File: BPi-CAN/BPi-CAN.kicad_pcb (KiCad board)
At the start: 2 copper layers, 100 x 100 mm, 123 parts, among them J1 RJ45, J2 RJ45, J3 RJ45, J4 RJ45, P1 BPi, P10 SPI, P11 SNIFFER, P12 CAN-Bus, P13 USB, P14 CAN-Bus, P15 POWER, P16 CAN, P17 CAN, P18 CAN, P19 TERM, P2 S88, P20 S88 CONN, P21 RS232 Con, P22 S88, P23 CONN_01X08, P24 CONN_01X03, P25 I2C-Bus, P3 CONN_02X04, P4 BPi Con, P5 TERM, P6 S88, P7 I2C-Bus, P8 RS485, P9 RS232, U1 MCP2562, U10 MCP2562, U11 6N137, U12 ISO1050, U13 FT230XS, U2 LM7805, U3 6N137, U4 6N137, U5 6N137, U6 6N137, U7 ADuM1251BR, U8 MAX3072E, U9 MAX3232

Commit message: small changes : mainly text
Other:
- board text added: "G"
- board text added: "V"
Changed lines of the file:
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@@
   (general
     (links 282)
-    (no_connects 0)
-    (area 86.872087 28.15 207.5 148.200001)
+    (no_connects 26)
+    (area 99.924999 39.924999 200.075001 140.075001)
     (thickness 1.6)
-    (drawings 101)
+    (drawings 105)
     (tracks 1773)
     (zones 0)
@@
     (at 172.085 62.23 90)
     (descr "5-way 3.5mm pitch terminal block, Phoenix PT series")
-    (fp_text reference P12 (at -1.778 -6.1595 360) (layer F.SilkS)
+    (fp_text reference P12 (at -2.921 -10.033 360) (layer F.SilkS)
       (effects (font (size 1.5 1.5) (thickness 0.3)))
     )
@@
     (descr "Through hole pin header")
     (tags "pin header")
-    (fp_text reference P7 (at -0.3556 -2.5273 90) (layer F.SilkS)
+    (fp_text reference P7 (at 0.635 -2.3495 90) (layer F.SilkS)
       (effects (font (size 1 1) (thickness 0.15)))
     )
@@
     (descr "Through hole pin header")
     (tags "pin header")
-    (fp_text reference P10 (at 0 -5.1 90) (layer F.SilkS)
+    (fp_text reference P10 (at -0.254 -3.429 90) (layer F.SilkS)
       (effects (font (size 1 1) (thickness 0.15)))
     )
@@
     )
   )
+  (gr_text SDA (at 178.054 96.393) (layer F.SilkS)
+    (effects (font (size 0.8 0.8) (thickness 0.2)))
+  )
+  (gr_text SCL (at 180.848 96.393) (layer F.SilkS)
+    (effects (font (size 0.8 0.8) (thickness 0.2)))
+  )
+  (gr_text G (at 185.42 99.06) (layer F.SilkS)
+    (effects (font (size 0.8 0.8) (thickness 0.2)))
+  )
+  (gr_text V (at 173.228 99.314) (layer F.SilkS)
+    (effects (font (size 0.8 0.8) (thickness 0.2)))
+  )
   (gr_text VCC (at 151.1046 119.3292) (layer F.SilkS)
     (effects (font (size 0.8 0.8) (thickness 0.2)))
@@
     (connect_pads (clearance 0.254))
     (min_thickness 0.254)
-    (fill yes (arc_segments 16) (thermal_gap 0.508) (thermal_bridge_width 0.508))
+    (fill (arc_segments 16) (thermal_gap 0.508) (thermal_bridge_width 0.508))
     (polygon
       (pts
@@
     (connect_pads (clearance 0.254))
     (min_thickness 0.254)
-    (fill yes (arc_segments 16) (thermal_gap 0.508) (thermal_bridge_width 0.508))
+    (fill (arc_segments 16) (thermal_gap 0.508) (thermal_bridge_width 0.508))
     (polygon
       (pts
@@
     (connect_pads (clearance 0.254))
     (min_thickness 0.254)
-    (fill yes (arc_segments 16) (thermal_gap 0.508) (thermal_bridge_width 0.508))
+    (fill (arc_segments 16) (thermal_gap 0.508) (thermal_bridge_width 0.508))
     (polygon
       (pts
@@
     (connect_pads (clearance 0.254))
     (min_thickness 0.254)
-    (fill yes (arc_segments 16) (thermal_gap 0.508) (thermal_bridge_width 0.508))
+    (fill (arc_segments 16) (thermal_gap 0.508) (thermal_bridge_width 0.508))
     (polygon
       (pts
@@
     (connect_pads (clearance 0.254))
     (min_thickness 0.254)
-    (fill yes (arc_segments 16) (thermal_gap 0.508) (thermal_bridge_width 0.508))
+    (fill (arc_segments 16) (thermal_gap 0.508) (thermal_bridge_width 0.508))
     (polygon
       (pts
@@
     (connect_pads (clearance 0.254))
     (min_thickness 0.254)
-    (fill yes (arc_segments 16) (thermal_gap 0.508) (thermal_bridge_width 0.508))
+    (fill (arc_segments 16) (thermal_gap 0.508) (thermal_bridge_width 0.508))
     (polygon
       (pts
@@
     (connect_pads (clearance 0.254))
     (min_thickness 0.254)
-    (fill yes (arc_segments 16) (thermal_gap 0.508) (thermal_bridge_width 0.508))
+    (fill (arc_segments 16) (thermal_gap 0.508) (thermal_bridge_width 0.508))
     (polygon
       (pts
@@
     (connect_pads (clearance 0.254))
     (min_thickness 0.254)
-    (fill yes (arc_segments 16) (thermal_gap 0.508) (thermal_bridge_width 0.508))
+    (fill (arc_segments 16) (thermal_gap 0.508) (thermal_bridge_width 0.508))
     (polygon
       (pts
@@
     (connect_pads (clearance 0.254))
     (min_thickness 0.254)
-    (fill yes (arc_segments 16) (thermal_gap 0.508) (thermal_bridge_width 0.508))
+    (fill (arc_segments 16) (thermal_gap 0.508) (thermal_bridge_width 0.508))
     (polygon
       (pts
@@
     (connect_pads (clearance 0.25))
     (min_thickness 0.254)
-    (fill yes (arc_segments 16) (thermal_gap 0.508) (thermal_bridge_width 0.508))
+    (fill (arc_segments 16) (thermal_gap 0.508) (thermal_bridge_width 0.508))
     (polygon
       (pts
@@
         (xy 165.989 81.788) (xy 172.339 81.788) (xy 172.339 88.646) (xy 174.625 90.424) (xy 175.387 91.186)
         (xy 175.387 96.012) (xy 173.609 96.012) (xy 171.323 100.076) (xy 137.795 100.076) (xy 137.795 75.438)
-        (xy 127.254 75.565) (xy 122.047 80.772) (xy 99.695 80.772) (xy 99.695 39.624) (xy 151.511 39.624)
-        (xy 151.511 51.054)
+        (xy 127.254 75.565) (xy 122.047 80.772) (xy 99.695 80.772) (xy 99.695 39.624) (xy 143.256 39.624)
+        (xy 143.256 51.054)
       )
     )
@@
     (connect_pads (clearance 0.25))
     (min_thickness 0.254)
-    (fill yes (arc_segments 16) (thermal_gap 0.508) (thermal_bridge_width 0.508))
+    (fill (arc_segments 16) (thermal_gap 0.508) (thermal_bridge_width 0.508))
     (polygon
       (pts
@@
         (xy 165.989 81.788) (xy 172.339 81.788) (xy 172.339 88.646) (xy 175.387 91.186) (xy 175.387 96.012)
         (xy 173.609 96.012) (xy 171.323 100.076) (xy 137.795 100.076) (xy 137.795 75.438) (xy 127.254 75.565)
-        (xy 122.047 80.772) (xy 99.695 80.772) (xy 99.695 39.624) (xy 151.511 39.624) (xy 151.511 51.054)
+        (xy 122.047 80.772) (xy 99.695 80.772) (xy 99.695 39.624) (xy 143.256 39.624) (xy 143.256 51.054)
       )
     )
@@
     (connect_pads (clearance 0.254))
     (min_thickness 0.254)
-    (fill yes (arc_segments 16) (thermal_gap 0.508) (thermal_bridge_width 0.508))
+    (fill (arc_segments 16) (thermal_gap 0.508) (thermal_bridge_width 0.508))
     (polygon
       (pts

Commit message: on the way to make the final release :-)
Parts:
- added P26: CONN_01X02, Pin_Headers:Pin_Header_Straight_1x02, F.Cu at (102.0, 98.0)
- moved C6 2.70 mm to (128.7, 98.0), turned to 90 degrees
- moved R8 2.10 mm to (123.6, 89.6)
- moved R9 1.91 mm to (123.6, 91.7)
- moved R6 1.44 mm to (114.0, 89.6)
- moved R7 1.08 mm to (114.0, 91.7)
- moved C7 0.58 mm to (107.8, 89.4)
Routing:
- net +5VD: track 82.1 -> 80.2 mm
- net /LOAD: track 26.5 -> 27.8 mm
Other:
- board text added: "V1.4 08/16"
- board text removed: "V1.3 05/16"

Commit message: next step to make the final release :-)
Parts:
- moved U3 3.36 mm to (109.2, 83.0)
- moved R4 2.76 mm to (142.0, 94.2)
- moved C5 2.55 mm to (128.7, 85.3)
- moved U4 2.53 mm to (135.5, 84.0)
- moved R3 1.13 mm to (142.0, 84.0)
- moved U6 0.95 mm to (119.4, 83.0)
- moved U5 0.51 mm to (135.5, 94.2)
- moved C7 0.25 mm to (107.5, 89.4)
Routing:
- net GND: track 257.7 -> 282.4 mm, vias 19 -> 21
- net GNDD: track 14.8 -> 31.1 mm, vias 0 -> 2
- net +5VD: track 80.2 -> 76.2 mm
- net /RESET: track 14.2 -> 10.5 mm
- net /GPIO2: track 49.7 -> 52.3 mm, vias 0 -> 1
- net +3V3: track 195.5 -> 197.7 mm
- net /LOAD: track 27.8 -> 26.4 mm
- net /DATA: track 12.4 -> 11.1 mm
- net +5V: track 94.3 -> 95.6 mm
- net /GPIO3: track 56.6 -> 55.5 mm
- net Net-(R4-Pad1): track 5.82 -> 4.80 mm
- net Net-(R2-Pad1): track 5.47 -> 4.50 mm
- net Net-(R6-Pad2): track 3.88 -> 2.93 mm
- net Net-(R3-Pad1): track 5.19 -> 4.60 mm
- net /UART3_TX: track 78.2 -> 78.0 mm, vias 4 -> 2

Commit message: next step to make the final release :-)
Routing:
- net /CVCC: track 94.7 -> 98.6 mm

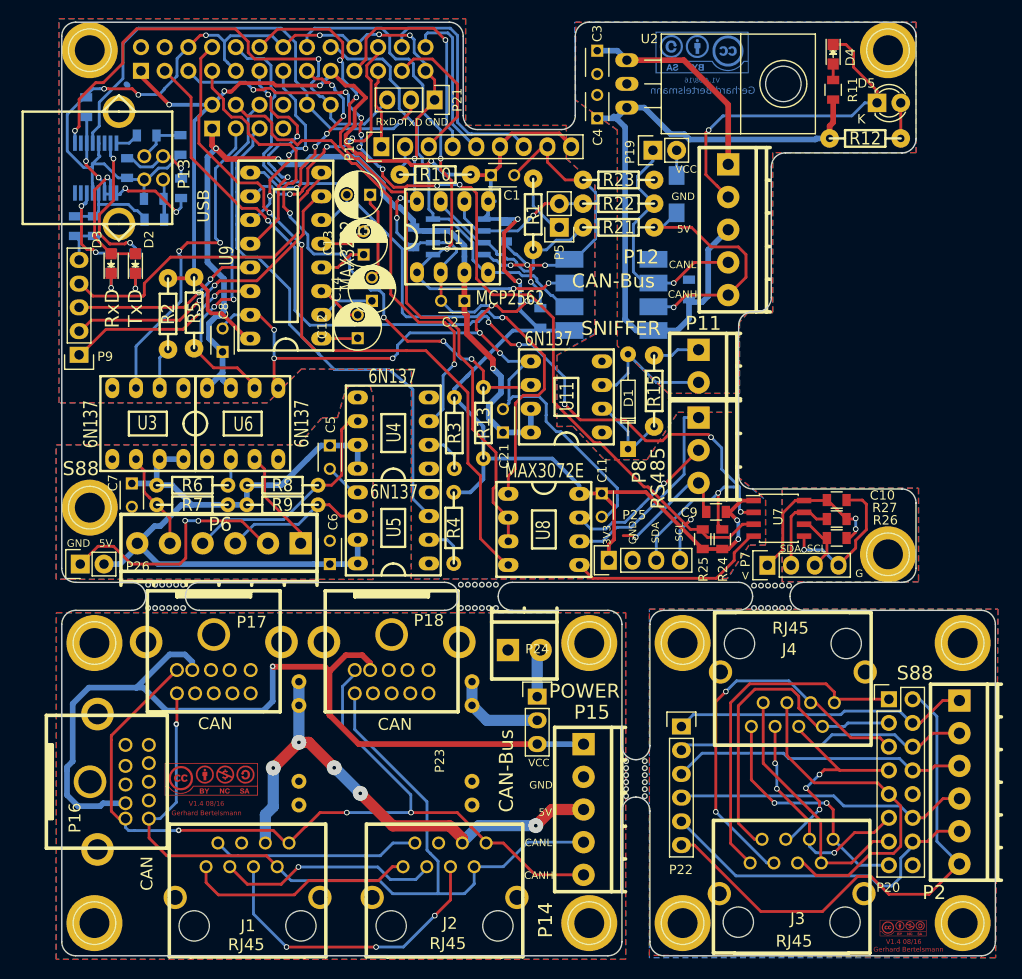
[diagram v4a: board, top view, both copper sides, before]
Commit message: reroute some part of the PCB
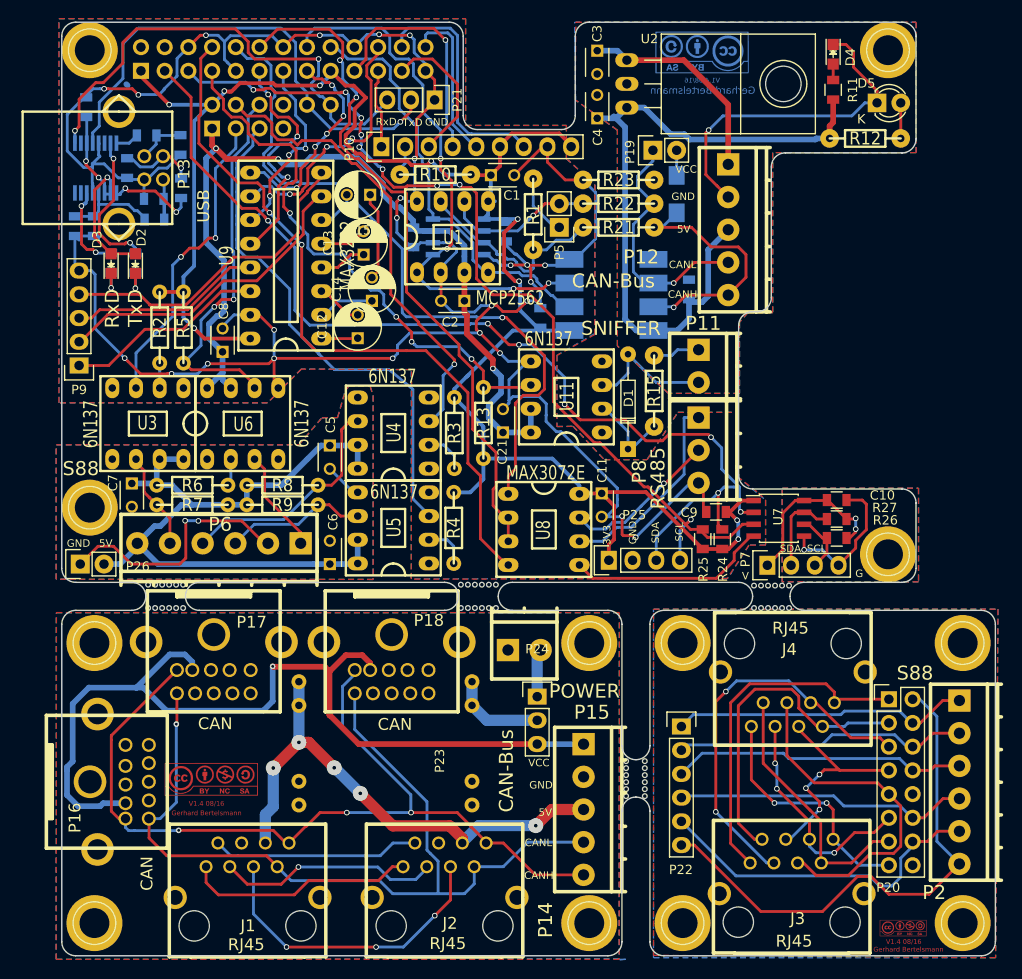
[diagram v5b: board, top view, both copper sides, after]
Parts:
- moved R5 1.96 mm to (113.0, 72.7)
- moved R2 1.71 mm to (110.5, 72.7)
- moved P9 1.14 mm to (101.9, 76.8)
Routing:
- net GND: track 282.4 -> 318.1 mm, vias 21 -> 25
- net +3V3: track 197.7 -> 200.7 mm, vias 8 -> 9
- net /GPIO4: track 38.3 -> 40.9 mm
- net Net-(R2-Pad1): track 4.50 -> 2.67 mm
- net /GPIO1: track 34.9 -> 33.2 mm
- net /GPIO2: track 52.3 -> 50.7 mm
- net /PH2: track 75.7 -> 74.3 mm
- net /I2C_SDA2: track 115.1 -> 114.2 mm
- net Net-(P9-Pad2): track 34.0 -> 34.5 mm, vias 2 -> 0
- net Net-(P9-Pad1): track 21.3 -> 21.7 mm, vias 2 -> 0
- net Net-(P9-Pad3): track 20.2 -> 20.6 mm, vias 2 -> 0

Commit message: more accurate copper pooring on S88 part
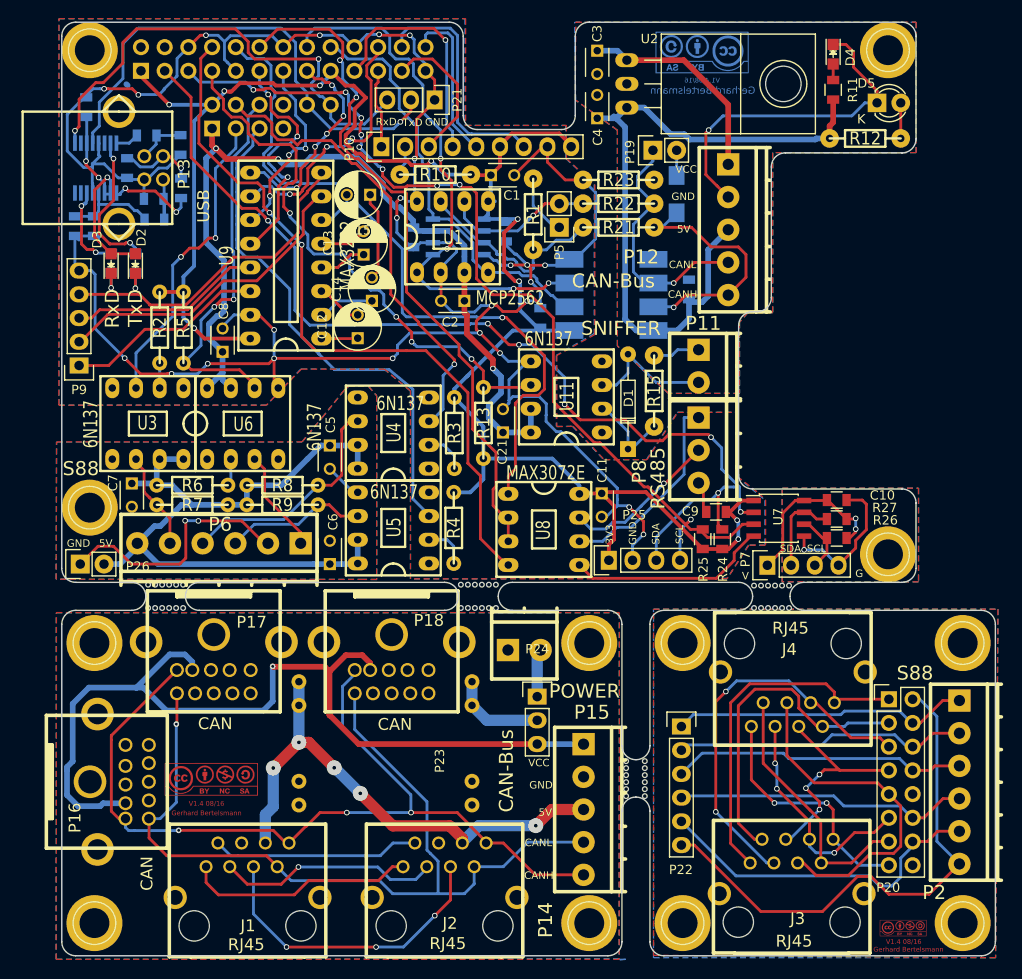
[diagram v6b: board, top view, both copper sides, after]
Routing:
- net GND: track 318.1 -> 312.2 mm
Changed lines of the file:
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@@
     (thickness 1.6)
     (drawings 107)
-    (tracks 1799)
+    (tracks 1798)
     (zones 0)
     (modules 124)
@@
     (mod_text_size 1 1)
     (mod_text_width 0.15)
-    (pad_size 1.6 1.6)
-    (pad_drill 0.8)
+    (pad_size 1.5 1.5)
+    (pad_drill 0.9)
     (pad_to_mask_clearance 0.2)
     (aux_axis_origin 0 0)
@@
       (effects (font (size 1.524 1.143) (thickness 0.28702)))
     )
-    (fp_text value 6N137 (at 6.3246 0.0127 90) (layer F.SilkS)
+    (fp_text value 6N137 (at 7.6835 0.381 90) (layer F.SilkS)
       (effects (font (size 1.524 1.143) (thickness 0.28702)))
     )
@@
       (effects (font (size 1 1) (thickness 0.15)))
     )
-    (fp_text value 100nF (at 1.25 2.5 270) (layer F.Fab)
+    (fp_text value 100nF (at 1.2192 -0.0889 270) (layer F.Fab)
       (effects (font (size 1 1) (thickness 0.15)))
     )
@@
     (tags "resistor 0805")
     (attr smd)
-    (fp_text reference C9 (at 2.8829 -0.0635 180) (layer F.SilkS)
+    (fp_text reference C9 (at 2.7559 0.0635 180) (layer F.SilkS)
       (effects (font (size 1 1) (thickness 0.15)))
     )
-    (fp_text value 100nF (at 0 2.1 180) (layer F.Fab)
+    (fp_text value 100nF (at -0.0381 0 180) (layer F.Fab)
       (effects (font (size 1 1) (thickness 0.15)))
     )
@@
       (effects (font (size 1.524 1.143) (thickness 0.28702)))
     )
-    (fp_text value 6N137 (at 6.0833 -0.1016 180) (layer F.SilkS)
+    (fp_text value 6N137 (at 3.175 0.762 180) (layer F.SilkS)
       (effects (font (size 1.524 1.143) (thickness 0.28702)))
     )
@@
       (effects (font (size 1 1) (thickness 0.15)))
     )
-    (fp_text value I2C-Bus (at 2.3622 4.2926 180) (layer F.Fab)
+    (fp_text value I2C-Bus (at -3.0099 3.8989 180) (layer F.Fab)
       (effects (font (size 1 1) (thickness 0.15)))
     )
@@
     (effects (font (size 0.8 0.8) (thickness 0.2)))
   )
-  (gr_text 3V3 (at 158.3944 94.9198 90) (layer F.SilkS)
+  (gr_text 3V3 (at 158.6865 94.869 90) (layer F.SilkS)
     (effects (font (size 0.8 0.8) (thickness 0.2)))
   )
-  (gr_text SCL (at 166.1414 94.5896 90) (layer F.SilkS)
+  (gr_text SCL (at 166.1795 94.869 90) (layer F.SilkS)
     (effects (font (size 0.8 0.8) (thickness 0.2)))
   )
-  (gr_text SDA (at 163.6014 94.6658 90) (layer F.SilkS)
+  (gr_text SDA (at 163.6395 94.8055 90) (layer F.SilkS)
     (effects (font (size 0.8 0.8) (thickness 0.2)))
   )
-  (gr_text GND (at 161.163 94.6658 90) (layer F.SilkS)
+  (gr_text GND (at 161.163 94.742 90) (layer F.SilkS)
     (effects (font (size 0.8 0.8) (thickness 0.2)))
   )
@@
   (segment (start 159.1564 91.7956) (end 157.8356 90.4748) (width 0.4064) (layer F.Cu) (net 1))
   (segment (start 158.5976 97.6376) (end 158.5976 95.9612) (width 0.4064) (layer F.Cu) (net 1))
+  (segment (start 159.512 91.7956) (end 160.6296 91.7956) (width 0.3048) (layer B.Cu) (net 2))
+  (segment (start 161.1376 96.0374) (end 161.1376 97.6376) (width 0.3048) (layer B.Cu) (net 2))
+  (segment (start 162.306 94.869) (end 161.1376 96.0374) (width 0.3048) (layer B.Cu) (net 2))
+  (via (at 162.306 94.869) (size 0.6) (drill 0.4) (layers F.Cu B.Cu) (net 2))
+  (segment (start 162.306 93.472) (end 162.306 94.869) (width 0.3048) (layer F.Cu) (net 2))
+  (segment (start 160.782 91.948) (end 162.306 93.472) (width 0.3048) (layer F.Cu) (net 2))
+  (via (at 160.782 91.948) (size 0.6) (drill 0.4) (layers F.Cu B.Cu) (net 2))
+  (segment (start 160.6296 91.7956) (end 160.782 91.948) (width 0.3048) (layer B.Cu) (net 2))
   (segment (start 111.76 77.6605) (end 111.335736 77.6605) (width 0.3048) (layer F.Cu) (net 2))
   (segment (start 108.425055 77.669901) (end 107.039156 76.284002) (width 0.3048) (layer F.Cu) (net 2))
@@
   (segment (start 101.4095 66.167) (end 101.854 66.6115) (width 0.3048) (layer B.Cu) (net 2))
   (via (at 106.739157 75.984003) (size 0.6) (drill 0.4) (layers F.Cu B.Cu) (net 2))
-  (segment (start 160.02 92.9005) (end 160.02 94.883999) (width 0.3048) (layer F.Cu) (net 2))
-  (segment (start 160.02 94.883999) (end 160.132001 94.996) (width 0.3048) (layer F.Cu) (net 2))
-  (segment (start 157.8356 92.9748) (end 159.9457 92.9748) (width 0.3048) (layer B.Cu) (net 2))
-  (segment (start 159.9457 92.9748) (end 160.02 92.9005) (width 0.3048) (layer B.Cu) (net 2))
-  (via (at 160.02 92.9005) (size 0.6) (drill 0.4) (layers F.Cu B.Cu) (net 2))
   (segment (start 122.174 76.581) (end 115.6335 76.581) (width 0.3048) (layer F.Cu) (net 2))
   (segment (start 122.7455 76.0095) (end 122.174 76.581) (width 0.3048) (layer F.Cu) (net 2))
@@
   (segment (start 115.443 41.402) (end 114.8334 41.402) (width 0.3048) (layer F.Cu) (net 2))
   (segment (start 167.315 89.352) (end 168.21 89.352) (width 0.3048) (layer B.Cu) (net 2))
-  (segment (start 161.29 94.996) (end 161.4805 95.1865) (width 0.3048) (layer F.Cu) (net 2))
-  (via (at 161.4805 95.1865) (size 0.6) (drill 0.4) (layers F.Cu B.Cu) (net 2))
-  (segment (start 161.4805 95.1865) (end 167.315 89.352) (width 0.3048) (layer B.Cu) (net 2))
-  (segment (start 160.132001 94.996) (end 161.29 94.996) (width 0.3048) (layer F.Cu) (net 2))
   (segment (start 118.4515 71.35) (end 120.19 71.35) (width 0.3048) (layer B.Cu) (net 2))
   (segment (start 117.221 72.5805) (end 118.4515 71.35) (width 0.3048) (layer B.Cu) (net 2))
@@
     (polygon
       (pts
-        (xy 132.334 99.6823) (xy 99.403 99.6688) (xy 99.403 85.269) (xy 125.403 85.269) (xy 127.8636 82.3722)
-        (xy 129.54 82.3595) (xy 130.4036 79.4258) (xy 130.7465 78.994) (xy 133.0325 78.994) (xy 133.35 80.01)
-        (xy 133.35 99.695)
+        (xy 132.334 99.6823) (xy 99.403 99.6688) (xy 99.441 84.963) (xy 125.73 84.963) (xy 127.8636 82.3722)
+        (xy 127.889 82.3595) (xy 130.2385 79.4385) (xy 130.7465 78.994) (xy 132.842 78.994) (xy 133.731 80.01)
+        (xy 133.731 99.695)
       )
     )
@@
         (xy 153.035 75.692) (xy 153.035 83.312) (xy 154.7622 83.2866) (xy 158.115 86.868) (xy 162.687 86.868)
         (xy 165.989 81.788) (xy 172.339 81.788) (xy 172.339 88.646) (xy 174.625 90.424) (xy 175.387 91.186)
-        (xy 175.387 96.012) (xy 173.609 96.012) (xy 171.2722 99.5934) (xy 137.4267 99.6569) (xy 137.4775 77.216)
-        (xy 125.6665 77.1525) (xy 122.047 80.772) (xy 99.695 80.772) (xy 99.695 39.624) (xy 143.256 39.624)
-        (xy 143.256 51.054)
+        (xy 175.387 96.012) (xy 173.609 96.012) (xy 171.2722 99.5934) (xy 137.3505 99.6315) (xy 137.3505 79.502)
+        (xy 134.5565 77.1525) (xy 125.6665 77.1525) (xy 121.92 81.026) (xy 99.695 81.026) (xy 99.695 39.624)
+        (xy 143.256 39.624) (xy 143.256 51.054)
       )
     )
@@
     (polygon
       (pts
-        (xy 151.511 51.054) (xy 154.051 51.054) (xy 154.051 54.61) (xy 157.099 57.404) (xy 157.099 73.3552)
-        (xy 153.035 75.692) (xy 153.035 83.312) (xy 154.7622 83.2866) (xy 158.115 86.868) (xy 162.687 86.868)
-        (xy 165.989 81.788) (xy 172.339 81.788) (xy 172.339 88.646) (xy 175.387 91.186) (xy 175.387 96.012)
-        (xy 173.609 96.012) (xy 171.3484 99.568) (xy 137.4394 99.6315) (xy 137.414 77.216) (xy 125.6665 77.1525)
-        (xy 122.047 80.772) (xy 99.695 80.772) (xy 99.695 39.624) (xy 143.256 39.624) (xy 143.256 51.054)
+        (xy 151.4475 51.054) (xy 153.9875 51.054) (xy 153.9875 54.61) (xy 157.0355 57.404) (xy 157.0355 73.3552)
+        (xy 152.9715 75.692) (xy 152.9715 83.312) (xy 154.6987 83.2866) (xy 158.0515 86.868) (xy 162.6235 86.868)
+        (xy 165.9255 81.788) (xy 172.2755 81.788) (xy 172.2755 88.646) (xy 175.3235 91.186) (xy 175.3235 96.012)
+        (xy 173.5455 96.012) (xy 171.2849 99.568) (xy 137.3505 99.6315) (xy 137.3505 79.502) (xy 134.493 77.1525)
+        (xy 125.603 77.1525) (xy 121.92 81.026) (xy 99.695 81.026) (xy 99.695 39.624) (xy 143.1925 39.624)
+        (xy 143.1925 51.054)
       )
     )
@@
     (polygon
       (pts
-        (xy 132.334 99.6823) (xy 99.403 99.6688) (xy 99.403 85.269) (xy 125.403 85.269) (xy 127.8636 82.3722)
-        (xy 129.54 82.3595) (xy 130.3655 79.4385) (xy 130.7465 78.994) (xy 133.0325 78.994) (xy 133.35 80.01)
-        (xy 133.35 99.695)
+        (xy 132.334 99.6823) (xy 99.403 99.6688) (xy 99.441 84.963) (xy 125.73 84.963) (xy 127.8636 82.3722)
+        (xy 127.889 82.3595) (xy 130.2385 79.4385) (xy 130.7465 78.994) (xy 132.842 78.994) (xy 133.731 80.01)
+        (xy 133.731 99.695)
       )
     )
